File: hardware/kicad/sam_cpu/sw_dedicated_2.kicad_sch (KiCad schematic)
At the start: 45 parts, among them J10 J10 SPEAKERS, U22 PCM5102A, U23 TDA2030A, U24 TDA2030A

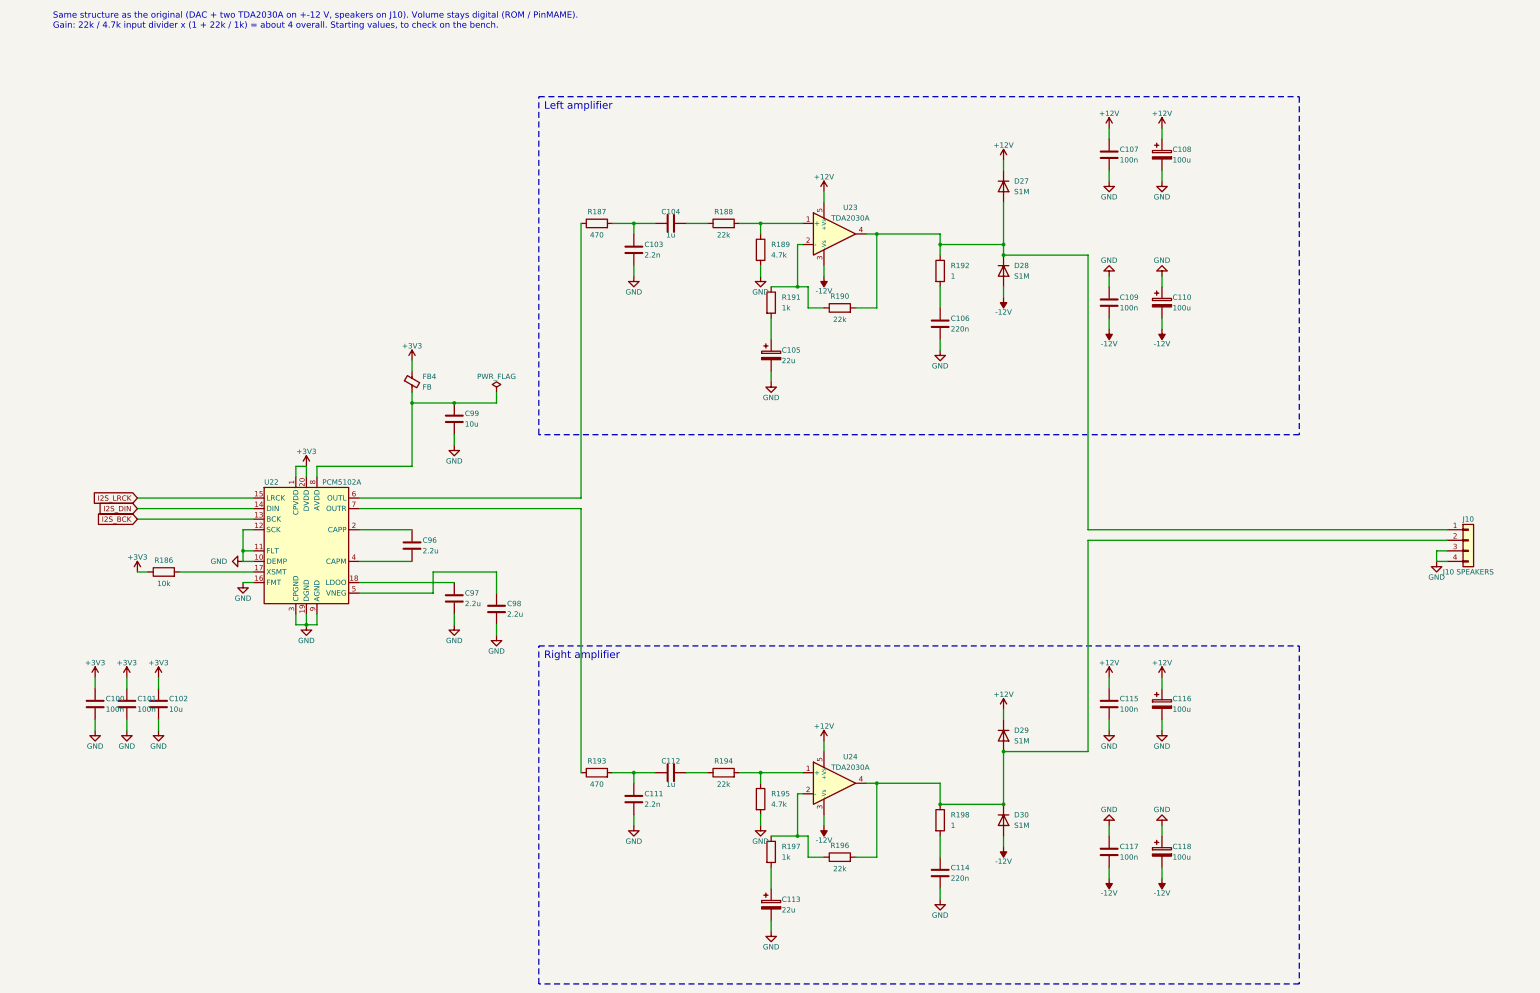
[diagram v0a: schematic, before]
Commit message: Redraw the schematic with wires (draft 0.2)
Every connection is now a wire, and each connector sits on the page of the
parts that drive or read it (Pi header with the RP2354B, J6/J12 with their
comparators and 74HC165, J1 with the 74HC595, J2/J3/J13 with their filters).
Signals between pages use global labels with page references. The Pi page is
merged into the MCU page; the Pi 4 sits on the 40-pin header J21.

ERC: 0 errors, 1 warning. Netlist check: 1266 pins, 299 nets, no differences.

Co-Authored-By: Claude Opus 5.5 (1M context) <noreply@anthropic.com>
Claude-Session: https://claude.ai/code/session_019DLTv1F2PjepjxqiUcAMKV
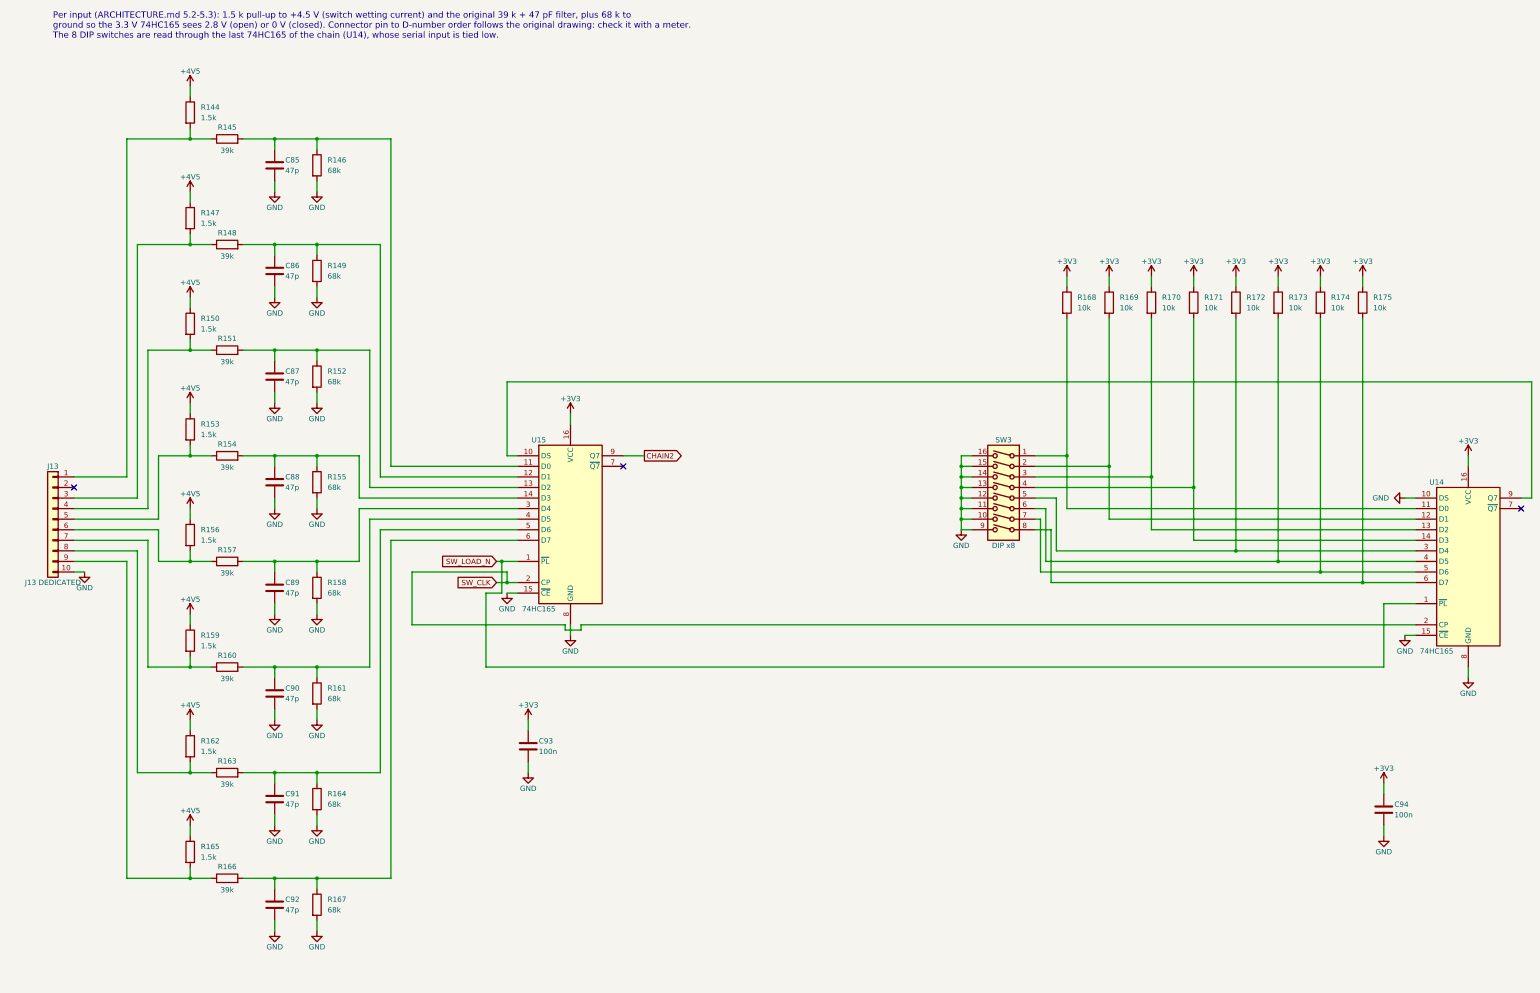
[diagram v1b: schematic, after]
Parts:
- removed C100, C101, C107, C109, C115, C117: 100n, Capacitor_SMD:C_0603_1608Metric, symbol Device:C
- removed C102, C99: 10u, Capacitor_SMD:C_0805_2012Metric, symbol Device:C
- removed C103, C111: 2.2n, Capacitor_SMD:C_0603_1608Metric, symbol Device:C
- removed C104, C112: 1u, Capacitor_SMD:C_0603_1608Metric, symbol Device:C
- removed C105, C113: 22u, Capacitor_SMD:CP_Elec_6.3x7.7, symbol Device:C_Polarized
- removed C106, C114: 220n, Capacitor_SMD:C_0603_1608Metric, symbol Device:C
- removed C108, C110, C116, C118: 100u, Capacitor_SMD:CP_Elec_6.3x7.7, symbol Device:C_Polarized
- removed C96, C97, C98: 2.2u, Capacitor_SMD:C_0805_2012Metric, symbol Device:C
- removed D27, D28, D29, D30: S1M, Diode_SMD:D_SMA, symbol Device:D
- removed FB4: FB, Inductor_SMD:L_0805_2012Metric, symbol Device:FerriteBead_Small
- removed J10: J10 SPEAKERS, Connector_Molex:Molex_KK-396_A-41791-0004_1x04_P3.96mm_Vertical, symbol Connector_Generic:Conn_01x04
- removed R186: 10k, Resistor_SMD:R_0603_1608Metric, symbol Device:R
- removed R187, R193: 470, Resistor_SMD:R_0603_1608Metric, symbol Device:R
- removed R188, R190, R194, R196: 22k, Resistor_SMD:R_0603_1608Metric, symbol Device:R
- removed R189, R195: 4.7k, Resistor_SMD:R_0603_1608Metric, symbol Device:R
- removed R191, R197: 1k, Resistor_SMD:R_0603_1608Metric, symbol Device:R
- removed R192, R198: 1, Resistor_SMD:R_1206_3216Metric, symbol Device:R
- removed U22: PCM5102A, Package_SO:TSSOP-20_4.4x6.5mm_P0.65mm, symbol Audio:PCM5102A
- removed U23, U24: TDA2030A, Package_TO_SOT_THT:TO-220-5_P3.4x3.7mm_StaggerOdd_Lead3.8mm_Vertical, symbol Amplifier_Audio:TDA2030
- added C85, C86, C87, C88, C89, C90, C91, C92: 47p, Capacitor_SMD:C_0603_1608Metric, symbol Device:C
- added C93, C94: 100n, Capacitor_SMD:C_0603_1608Metric, symbol Device:C
- added J13: J13 DEDICATED, Connector_Molex:Molex_KK-254_AE-6410-10A_1x10_P2.54mm_Vertical, symbol Connector_Generic:Conn_01x10
- added R144, R147, R150, R153, R156, R159, R162, R165: 1.5k, Resistor_SMD:R_0603_1608Metric, symbol Device:R
- added R145, R148, R151, R154, R157, R160, R163, R166: 39k, Resistor_SMD:R_0603_1608Metric, symbol Device:R
- added R146, R149, R152, R155, R158, R161, R164, R167: 68k, Resistor_SMD:R_0603_1608Metric, symbol Device:R
- added R168, R169, R170, R171, R172, R173, R174, R175: 10k, Resistor_SMD:R_0603_1608Metric, symbol Device:R
- added SW3: DIP x8, Button_Switch_THT:SW_DIP_SPSTx08_Slide_9.78x22.5mm_W7.62mm_P2.54mm, symbol Switch:SW_DIP_x08
- added U14, U15: 74HC165, Package_SO:SOIC-16_3.9x9.9mm_P1.27mm, symbol 74xx:74HC165
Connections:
- net +3V3: now also C93.1, C94.1, R168.1, R169.1, R170.1, R171.1, R172.1, R173.1, R174.1, R175.1, U14.16 (VCC), U15.16 (VCC)
- net GND: now also C85.2, C86.2, C87.2, C88.2, C89.2, C90.2, C91.2, C92.2, C93.2, C94.2, J13.10 (Pin_10), R146.2, R149.2, R152.2, R155.2, R158.2, R161.2, R164.2, R167.2, SW3.10, SW3.11, SW3.12, SW3.13, SW3.14, SW3.15, SW3.16, SW3.9, U14.10 (DS), U14.15 (~{CE}), U14.8 (GND), U15.15 (~{CE}), U15.8 (GND)
- new net: J13.6 (Pin_6), R156.2, R157.1
- new net: C89.1, R157.2, R158.1, U15.3 (D4)
- new net: C90.1, R160.2, R161.1, U15.4 (D5)
- new net: C92.1, R166.2, R167.1, U15.6 (D7)
- new net: J13.3 (Pin_3), R147.2, R148.1
- new net: C86.1, R148.2, R149.1, U15.12 (D1)
- new net: C87.1, R151.2, R152.1, U15.13 (D2)
- new net: C91.1, R163.2, R164.1, U15.5 (D6)
- new net: J13.1 (Pin_1), R144.2, R145.1
- new net: R170.2, SW3.3, U14.13 (D2)
- new net: R173.2, SW3.6, U14.4 (D5)
- new net: J13.8 (Pin_8), R162.2, R163.1
- new net: J13.7 (Pin_7), R159.2, R160.1
- new net: J13.4 (Pin_4), R150.2, R151.1
- new net: J13.5 (Pin_5), R153.2, R154.1
- new net: J13.9 (Pin_9), R165.2, R166.1
- new net: R169.2, SW3.2, U14.12 (D1)
- new net: R168.2, SW3.1, U14.11 (D0)
- new net: R171.2, SW3.4, U14.14 (D3)
- new net: R172.2, SW3.5, U14.3 (D4)
- new net: R174.2, SW3.7, U14.5 (D6)
- new net: R175.2, SW3.8, U14.6 (D7)
- new net: U14.9 (Q7), U15.10 (DS)
- new net: C88.1, R154.2, R155.1, U15.14 (D3)
- new net: C85.1, R145.2, R146.1, U15.11 (D0)
- new net +4V5: R144.1, R147.1, R150.1, R153.1, R156.1, R159.1, R162.1, R165.1
- new net CHAIN2: U15.9 (Q7)
- new net SW_CLK: U14.2 (CP), U15.2 (CP)
- new net SW_LOAD_N: U14.1 (~{PL}), U15.1 (~{PL})
- no-connect marks 0 -> 3
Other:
- note added: "Per input (ARCHITECTURE.md 5.2-5.3): 1.5 k pull-up to +4.5 V (switch wetting current) and the original 39 k + 47 pF filter, plus 68 k to ground so the 3.3 V 74HC165 sees 2.8 V (open) or 0 V (closed). Connector pin to D-number order follows the original drawing: check it with a meter. The 8 DIP switches are read through the last 74HC165 of the chain (U14), whose serial input is tied low."
- note removed: "Left amplifier"
- note removed: "Right amplifier"
- note removed: "Same structure as the original (DAC + two TDA2030A on +-12 V, speakers on J10). Volume stays digital (ROM / PinMAME). Gain: 22k / 4.7k input divider x (1 + 22k / 1k) = about 4 overall. Starting values, to check on the bench."
- title: Audio: Pi I2S -> PCM5102A -> 2 x TDA2030A on +-12 V -> J10 -> Dedicated switches D17-D24 (J13) and DIP switches

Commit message: Use 3.96 mm KK-396 footprints for the switch harness connectors
J1, J2, J3, J6, J12 and J13 are 0.156" headers on the original board, so
the existing harness plugs need KK-396, as already used for J10 and J11.

Co-Authored-By: Claude Opus 5.5 (1M context) <noreply@anthropic.com>
Claude-Session: https://claude.ai/code/session_019DLTv1F2PjepjxqiUcAMKV
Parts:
- J13: footprint Connector_Molex:Molex_KK-254_AE-6410-10A_1x10_P2.54mm_Vertical -> Connector_Molex:Molex_KK-396_A-41791-0010_1x10_P3.96mm_Vertical
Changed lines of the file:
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@@
 			)
 		)
-		(property "Footprint" "Connector_Molex:Molex_KK-254_AE-6410-10A_1x10_P2.54mm_Vertical"
+		(property "Footprint" "Connector_Molex:Molex_KK-396_A-41791-0010_1x10_P3.96mm_Vertical"
 			(at 15.24 137.16 0)
 			(hide yes)

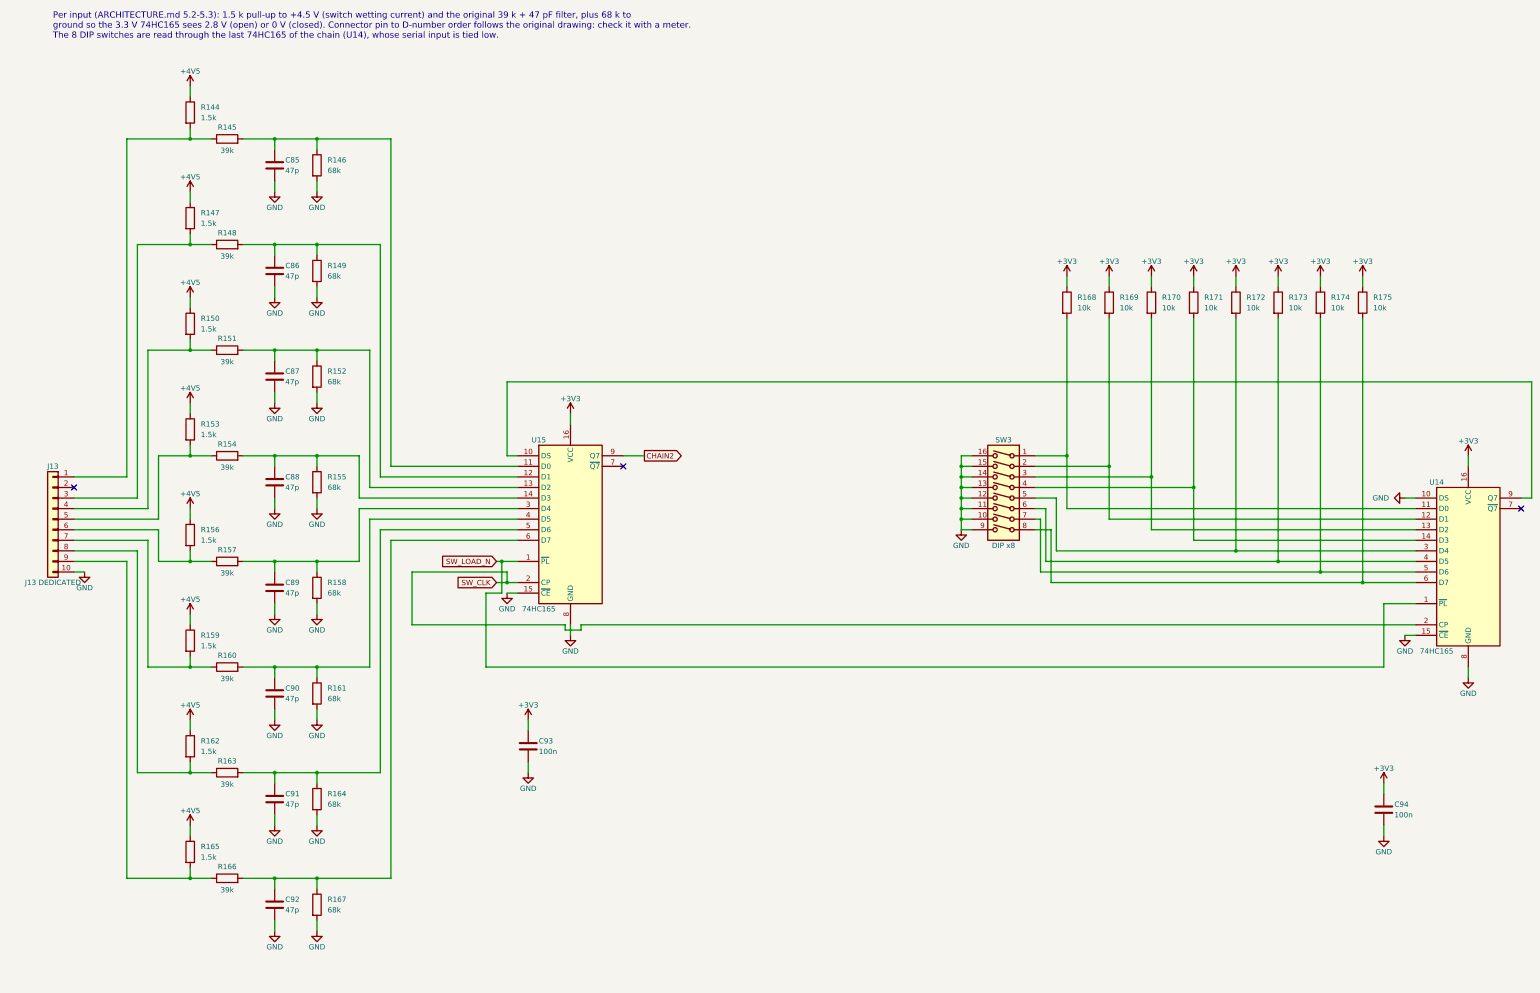
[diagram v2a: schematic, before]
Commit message: DIP switch block not loaded; larger schematic text
c30: SW3, R168-R175, U14 and C93 flagged DNP (schematic and board).
c31: schematic text 1.27 -> 1.6 mm (pins 1.5 mm), intersheet refs moved out.

Co-Authored-By: Claude Opus 5.5 (1M context) <noreply@anthropic.com>
Claude-Session: https://claude.ai/code/session_01ExuDVoDDDHhVWjb8EwVzYb
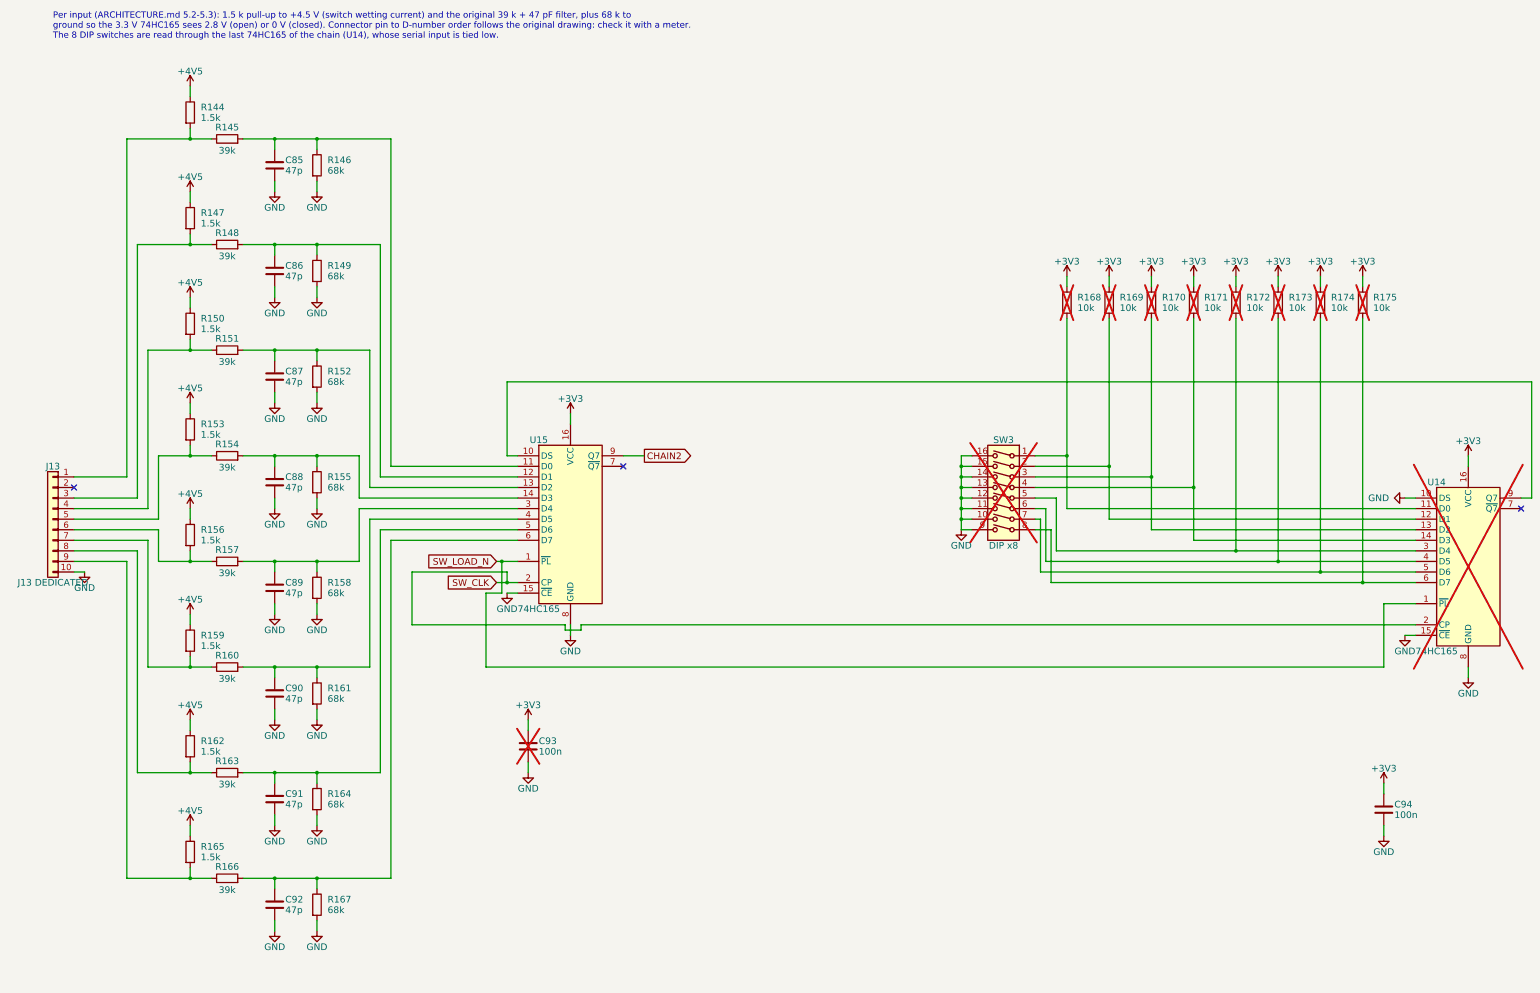
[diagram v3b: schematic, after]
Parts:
- C93, R168, R169, R170, R171, R172, R173, R174, R175, SW3, U14: now not fitted
